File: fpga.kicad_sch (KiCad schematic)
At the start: 2 parts

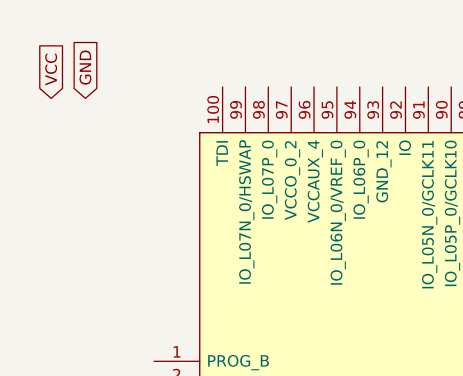
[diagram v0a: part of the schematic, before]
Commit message: now using correct VCC and GND symbols
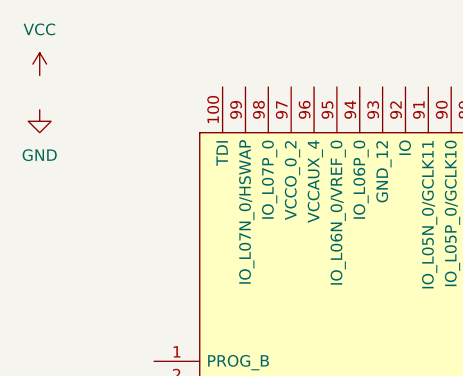
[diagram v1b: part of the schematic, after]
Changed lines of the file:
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@@
 (kicad_sch (version 20211123) (generator eeschema)
   (paper "A4")
-  (global_label "GND" (shape input) (at 24.13 22.86 90) (fields_autoplaced)
-    (effects (font (size 1.27 1.27)) (justify left))
-    (property "Intersheet References" "${INTERSHEET_REFS}" (id 0) (at 24.0506 16.5764 90)
-      (effects (font (size 1.27 1.27)) (justify left) hide)
-    )
-  )
-  (global_label "VCC" (shape input) (at 20.32 22.86 90) (fields_autoplaced)
-    (effects (font (size 1.27 1.27)) (justify left))
-    (property "Intersheet References" "${INTERSHEET_REFS}" (id 0) (at 20.2406 16.8183 90)
-      (effects (font (size 1.27 1.27)) (justify left) hide)
-    )
-  )
   (symbol (lib_id "fpga:XC3S250E-4VQG100C") (at 31.75 52.07 0) (unit 1)
     (in_bom yes) (on_board yes) (fields_autoplaced)
@@
     (pin "99")
   )
+  (symbol (lib_id "power:GND") (at 19.05 24.13 0) (unit 1)
+    (in_bom yes) (on_board yes) (fields_autoplaced)
+    (property "Reference" "#PWR?" (id 0) (at 19.05 30.48 0)
+      (effects (font (size 1.27 1.27)) hide)
+    )
+    (property "Value" "GND" (id 1) (at 19.05 29.21 0))
+    (property "Footprint" "" (id 2) (at 19.05 24.13 0)
+      (effects (font (size 1.27 1.27)) hide)
+    )
+    (property "Datasheet" "" (id 3) (at 19.05 24.13 0)
+      (effects (font (size 1.27 1.27)) hide)
+    )
+    (pin "1")
+  )
+  (symbol (lib_id "power:VCC") (at 19.05 20.32 0) (unit 1)
+    (in_bom yes) (on_board yes) (fields_autoplaced)
+    (property "Reference" "#PWR?" (id 0) (at 19.05 24.13 0)
+      (effects (font (size 1.27 1.27)) hide)
+    )
+    (property "Value" "VCC" (id 1) (at 19.05 15.24 0))
+    (property "Footprint" "" (id 2) (at 19.05 20.32 0)
+      (effects (font (size 1.27 1.27)) hide)
+    )
+    (property "Datasheet" "" (id 3) (at 19.05 20.32 0)
+      (effects (font (size 1.27 1.27)) hide)
+    )
+    (pin "1")
+  )
   (symbol (lib_id "fpga:W25N512GVEIG") (at 208.28 26.67 0) (unit 1)

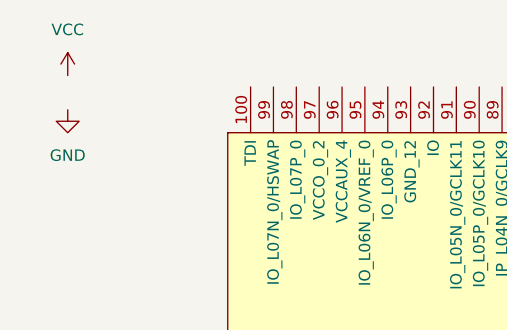
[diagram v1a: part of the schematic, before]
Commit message: added esp32 schematic && updated supply symbols
Signed-off-by: Tobias Gent <gent.tobias@gmail.com>
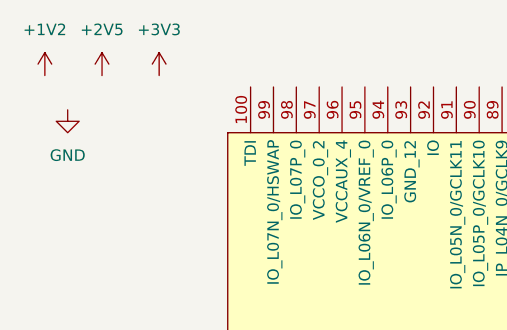
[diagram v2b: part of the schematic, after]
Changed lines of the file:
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@@
 (kicad_sch (version 20211123) (generator eeschema)
   (paper "A4")
+  (symbol (lib_id "power:+3V3") (at 29.21 20.32 0) (unit 1)
+    (in_bom yes) (on_board yes) (fields_autoplaced)
+    (property "Reference" "#PWR?" (id 0) (at 29.21 24.13 0)
+      (effects (font (size 1.27 1.27)) hide)
+    )
+    (property "Value" "+3V3" (id 1) (at 29.21 15.24 0))
+    (property "Footprint" "" (id 2) (at 29.21 20.32 0)
+      (effects (font (size 1.27 1.27)) hide)
+    )
+    (property "Datasheet" "" (id 3) (at 29.21 20.32 0)
+      (effects (font (size 1.27 1.27)) hide)
+    )
+    (pin "1")
+  )
+  (symbol (lib_id "power:+1V2") (at 16.51 20.32 0) (unit 1)
+    (in_bom yes) (on_board yes) (fields_autoplaced)
+    (property "Reference" "#PWR?" (id 0) (at 16.51 24.13 0)
+      (effects (font (size 1.27 1.27)) hide)
+    )
+    (property "Value" "+1V2" (id 1) (at 16.51 15.24 0))
+    (property "Footprint" "" (id 2) (at 16.51 20.32 0)
+      (effects (font (size 1.27 1.27)) hide)
+    )
+    (property "Datasheet" "" (id 3) (at 16.51 20.32 0)
+      (effects (font (size 1.27 1.27)) hide)
+    )
+    (pin "1")
+  )
   (symbol (lib_id "fpga:XC3S250E-4VQG100C") (at 31.75 52.07 0) (unit 1)
     (in_bom yes) (on_board yes) (fields_autoplaced)
@@
     (pin "1")
   )
-  (symbol (lib_id "power:VCC") (at 19.05 20.32 0) (unit 1)
+  (symbol (lib_id "power:+2V5") (at 22.86 20.32 0) (unit 1)
     (in_bom yes) (on_board yes) (fields_autoplaced)
-    (property "Reference" "#PWR?" (id 0) (at 19.05 24.13 0)
+    (property "Reference" "#PWR?" (id 0) (at 22.86 24.13 0)
       (effects (font (size 1.27 1.27)) hide)
     )
-    (property "Value" "VCC" (id 1) (at 19.05 15.24 0))
-    (property "Footprint" "" (id 2) (at 19.05 20.32 0)
+    (property "Value" "+2V5" (id 1) (at 22.86 15.24 0))
+    (property "Footprint" "" (id 2) (at 22.86 20.32 0)
       (effects (font (size 1.27 1.27)) hide)
     )
-    (property "Datasheet" "" (id 3) (at 19.05 20.32 0)
+    (property "Datasheet" "" (id 3) (at 22.86 20.32 0)
       (effects (font (size 1.27 1.27)) hide)
     )

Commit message: fpga powa
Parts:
- added C? (x11): 100n, symbol Device:C_Small
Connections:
- net +1V2: now also IC?.28 (VCCINT_2), IC?.56 (VCCINT_3), IC?.6 (VCCINT_1), IC?.80 (VCCINT_4), C?.1, C?.1, C?.1, C?.1
- net +2V5: now also IC?.21 (VCCAUX_1), IC?.46 (VCCAUX_2), IC?.74 (VCCAUX_3), IC?.96 (VCCAUX_4), C?.1, C?.1, C?.1, C?.1
- net +3V3: now also IC?.20 (VCCO_3_2), IC?.31 (VCCO_2_1), IC?.45 (VCCO_2_2), IC?.55 (VCCO_1_1), IC?.73 (VCCO_1_2), IC?.8 (VCCO_3_1), IC?.82 (VCCO_0_1), IC?.97 (VCCO_0_2), C?.1, C?.1, C?.1
- net GND: now also IC?.14 (GND_2), IC?.19 (GND_3), IC?.29 (GND_4), IC?.37 (GND_5), IC?.52 (GND_6), IC?.59 (GND_7), IC?.64 (GND_8), IC?.7 (GND_1), IC?.72 (GND_9), IC?.81 (GND_10), IC?.87 (GND_11), IC?.93 (GND_12), C?.2, C?.2, C?.2, C?.2, C?.2, C?.2, C?.2, C?.2, C?.2, C?.2, C?.2
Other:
- note added: "VCCAUX"
- note added: "VCCINT"
- note added: "VCCO"
- moved on the sheet: IC?

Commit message: added hdmi
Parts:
- added J?: HDMI_A, symbol Connector:HDMI_A
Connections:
- no-connect marks 0 -> 1
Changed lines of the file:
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@@
   (junction (at 85.09 30.48) (diameter 0) (color 0 0 0 0)
   )
+  (no_connect (at 220.98 106.68))
   (wire (pts (xy 43.18 30.48) (xy 43.18 36.83))
     (stroke (width 0) (type default) (color 0 0 0 0))
@@
     (pin "2")
   )
+  (symbol (lib_id "Connector:HDMI_A") (at 231.14 91.44 0) (unit 1)
+    (in_bom yes) (on_board yes) (fields_autoplaced)
+    (property "Reference" "J?" (id 0) (at 242.062 90.5315 0)
+      (effects (font (size 1.27 1.27)) (justify left))
+    )
+    (property "Value" "HDMI_A" (id 1) (at 242.062 93.3066 0)
+      (effects (font (size 1.27 1.27)) (justify left))
+    )
+    (property "Footprint" "" (id 2) (at 231.775 91.44 0)
+      (effects (font (size 1.27 1.27)) hide)
+    )
+    (property "Datasheet" "https://en.wikipedia.org/wiki/HDMI" (id 3) (at 231.775 91.44 0)
+      (effects (font (size 1.27 1.27)) hide)
+    )
+    (property "MNR" "179-HD04-19-TH-TR" (id 4) (at 231.14 91.44 0)
+      (effects (font (size 1.27 1.27)) hide)
+    )
+    (pin "1")
+    (pin "10")
+    (pin "11")
+    (pin "12")
+    (pin "13")
+    (pin "14")
+    (pin "15")
+    (pin "16")
+    (pin "17")
+    (pin "18")
+    (pin "19")
+    (pin "2")
+    (pin "3")
+    (pin "4")
+    (pin "5")
+    (pin "6")
+    (pin "7")
+    (pin "8")
+    (pin "9")
+    (pin "SH")
+  )
   (symbol (lib_id "Device:C_Small") (at 138.43 81.28 0) (unit 1)

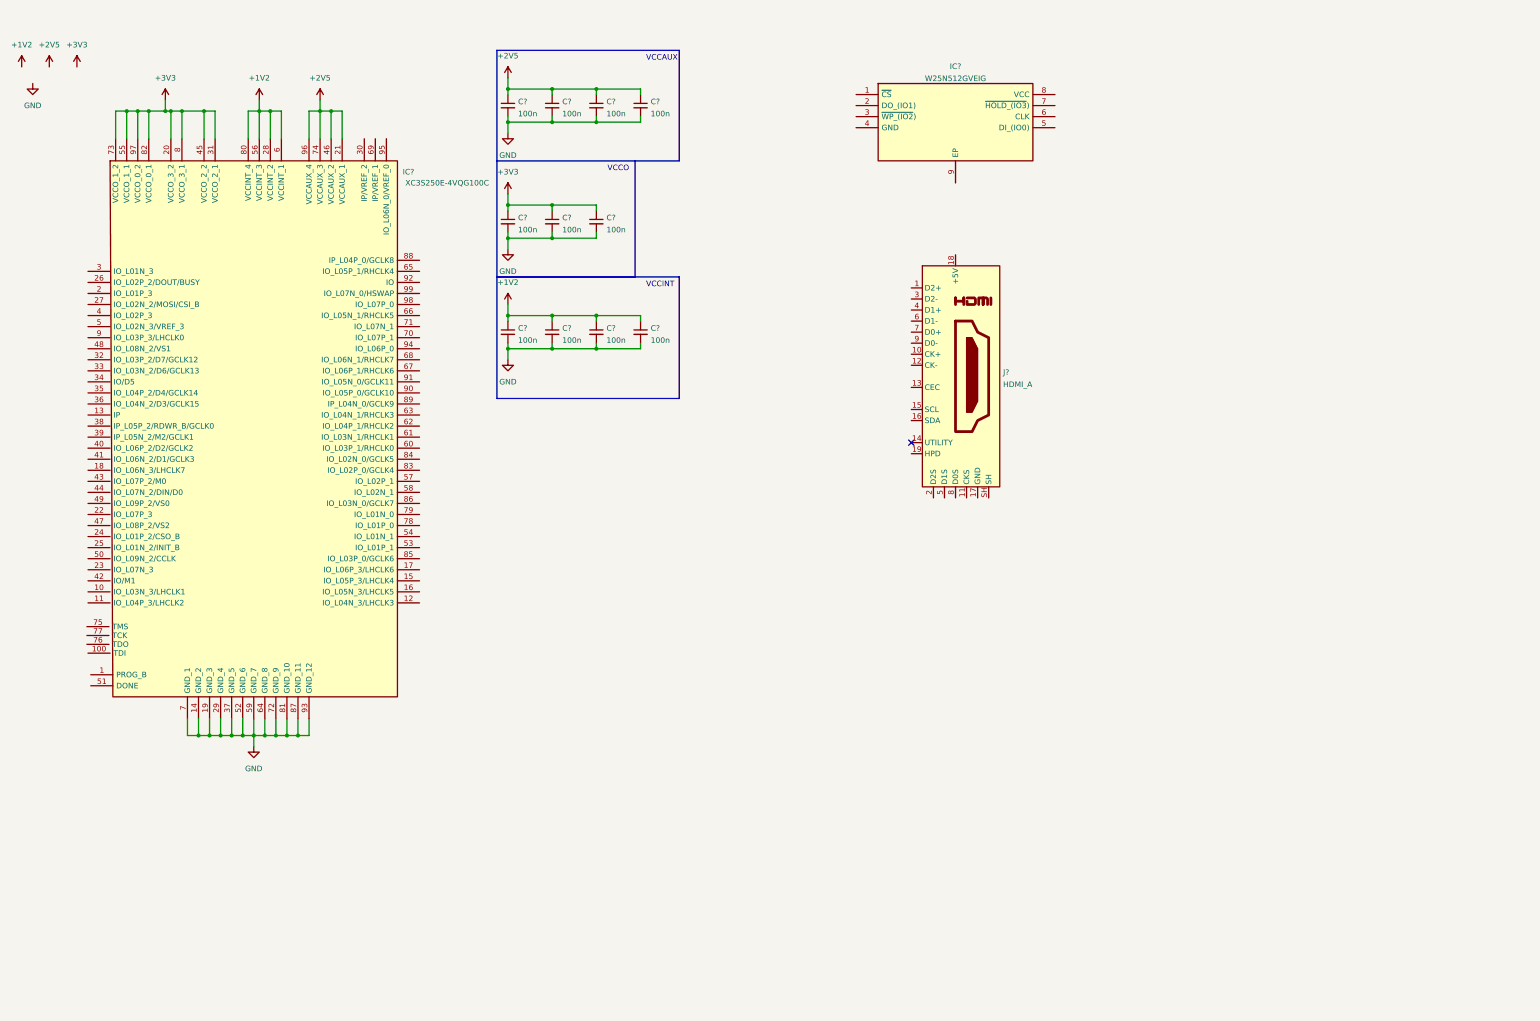
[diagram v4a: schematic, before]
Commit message: Add fpga HDMI basic components
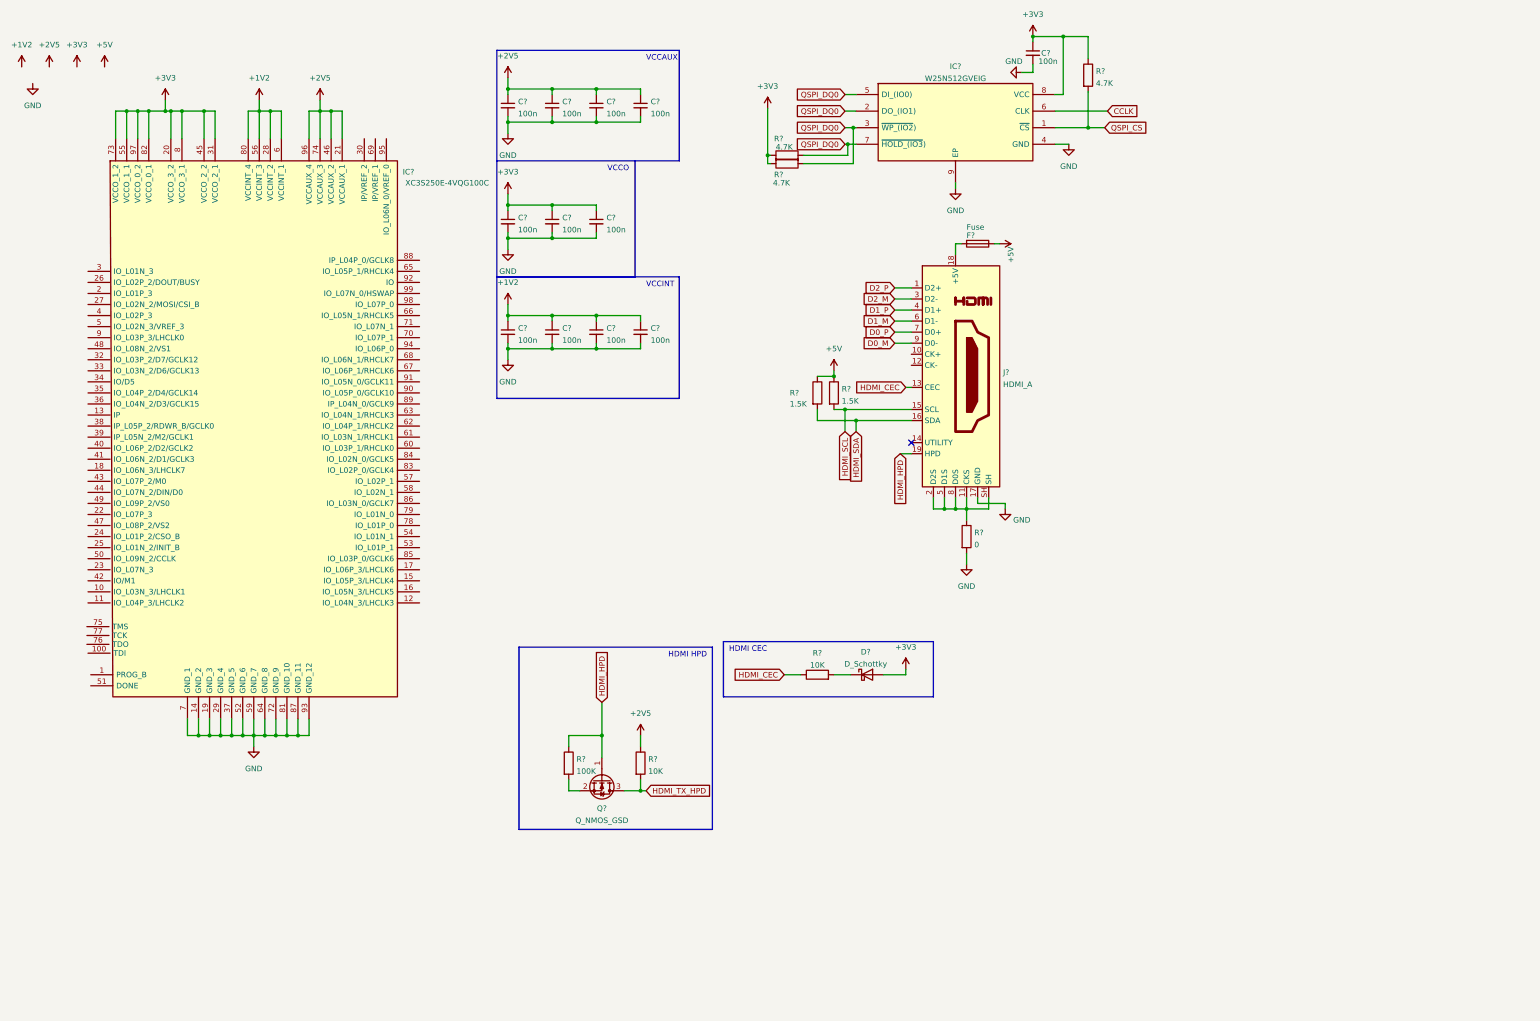
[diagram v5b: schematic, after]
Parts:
- added C?: 100n, symbol Device:C_Small
- added D?: D_Schottky, symbol Device:D_Schottky
- added F?: Fuse, symbol Device:Fuse
- added Q?: Q_NMOS_GSD, symbol Device:Q_NMOS_GSD
- added R? (x2): 1.5K, symbol Device:R
- added R?: 100K, symbol Device:R
- added R? (x3): 4.7K, symbol Device:R
- added R? (x2): 10K, symbol Device:R
- added R?: 0, symbol Device:R
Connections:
- net +2V5: now also R?.1
- net +3V3: now also IC?.8 (VCC), C?.1, D?.2 (A), R?.1, R?.1, R?.2
- net GND: now also IC?.4 (GND), IC?.9 (EP), J?.17 (GND), C?.2, R?.2
- net QSPI_CS: now reaches IC?.1 (~{CS})
- net QSPI_CS: now also R?.2
- net QSPI_DQ0: now reaches IC?.2 (DO_(IO1))
- net QSPI_DQ0: now also IC?.3 (~{WP_(IO2})), IC?.5 (DI_(IO0)), IC?.7 (~{HOLD_(IO3})), R?.1, R?.2
- net CCLK: now reaches IC?.6 (CLK)
- net D2_P: now reaches J?.1 (D2+)
- net at J?.11 (CKS): now also J?.2 (D2S), J?.5 (D1S), J?.8 (D0S), J?.SH, R?.1
- net HDMI_CEC: now reaches J?.13 (CEC)
- net HDMI_CEC: now also R?.1
- net HDMI_SCL: now reaches J?.15 (SCL)
- net HDMI_SCL: now also R?.2
- net HDMI_SDA: now reaches J?.16 (SDA)
- net HDMI_SDA: now also R?.2
- net at J?.18 (+5V): now also F?.2
- net HDMI_HPD: now reaches J?.19 (HPD)
- net HDMI_HPD: now also Q?.1 (G), R?.1
- net D2_M: now reaches J?.3 (D2-)
- net D1_P: now reaches J?.4 (D1+)
- net D1_M: now reaches J?.6 (D1-)
- net D0_P: now reaches J?.7 (D0+)
- net D0_M: now reaches J?.9 (D0-)
- new net: Q?.2 (S), R?.2
- new net: D?.1 (K), R?.2
- new net +5V: F?.1, R?.1, R?.1
- new net HDMI_TX_HPD: Q?.3 (D), R?.2
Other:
- note added: "HDMI CEC"
- note added: "HDMI HPD"

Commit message: added new IC to fpga.kicad_sch && changed sheet size of fpga.kicad_sch to A3
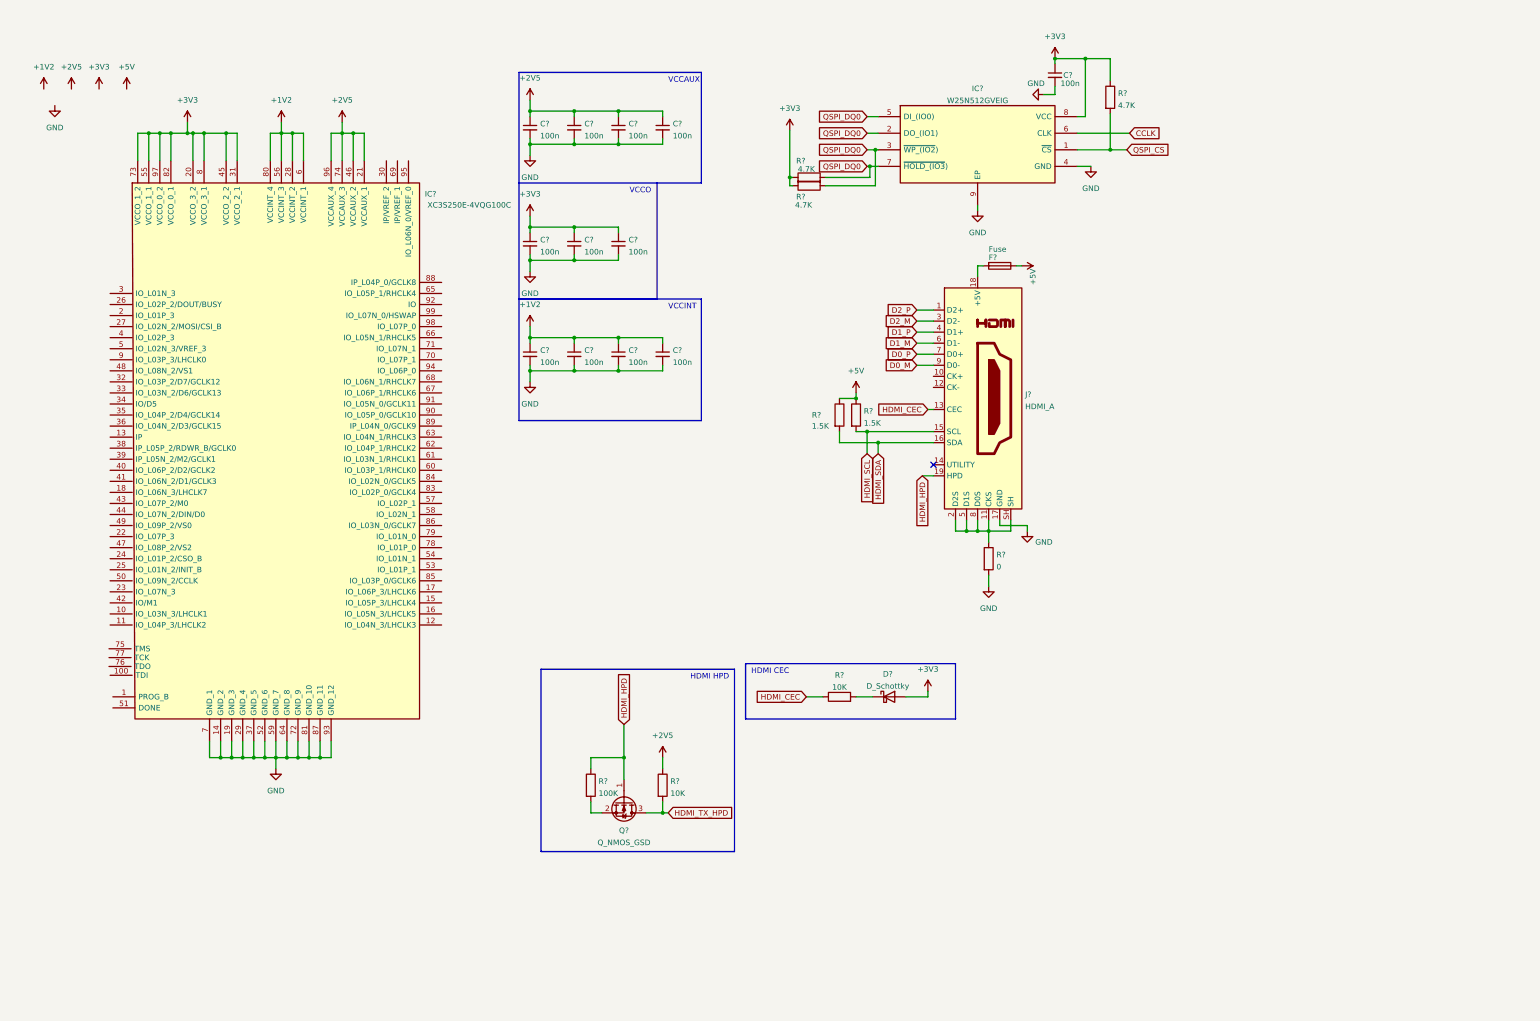
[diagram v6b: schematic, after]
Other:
- moved on the sheet: C?, D?, F?, IC?, J?, Q?, R?
